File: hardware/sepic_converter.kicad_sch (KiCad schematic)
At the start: 8 parts, among them Q1 IRF640N, U1 TC4422

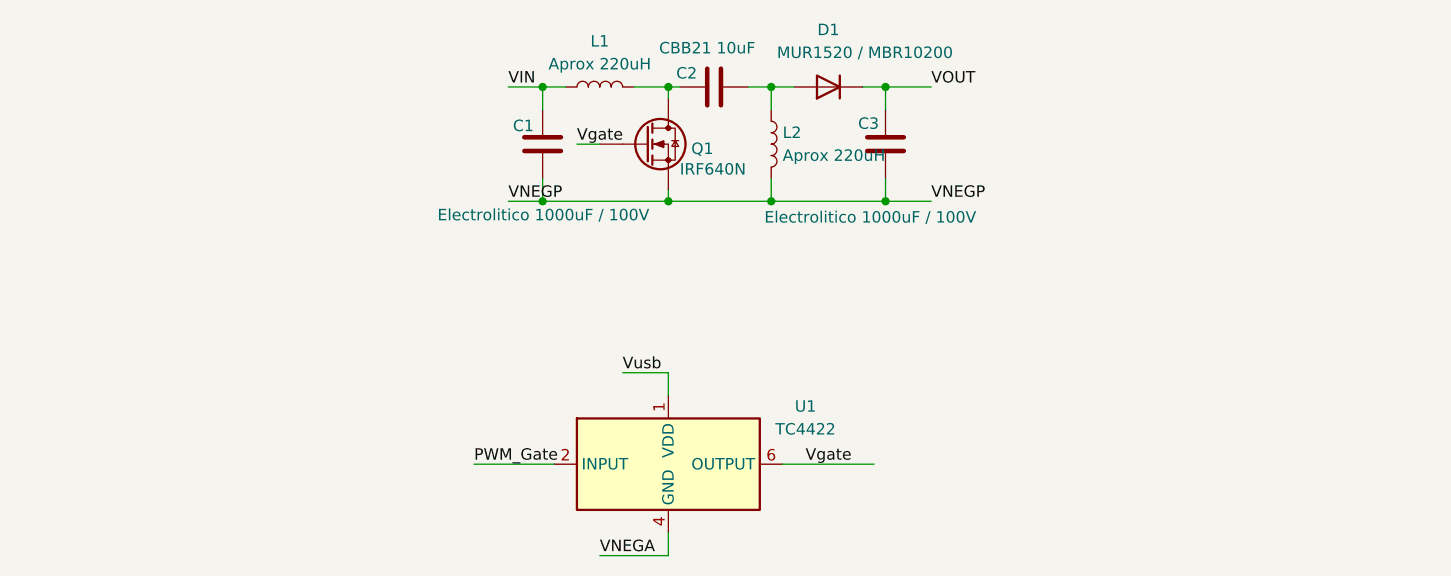
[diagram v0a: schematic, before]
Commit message: HW: Footprints, Descriptions and LCSC part number added to sch
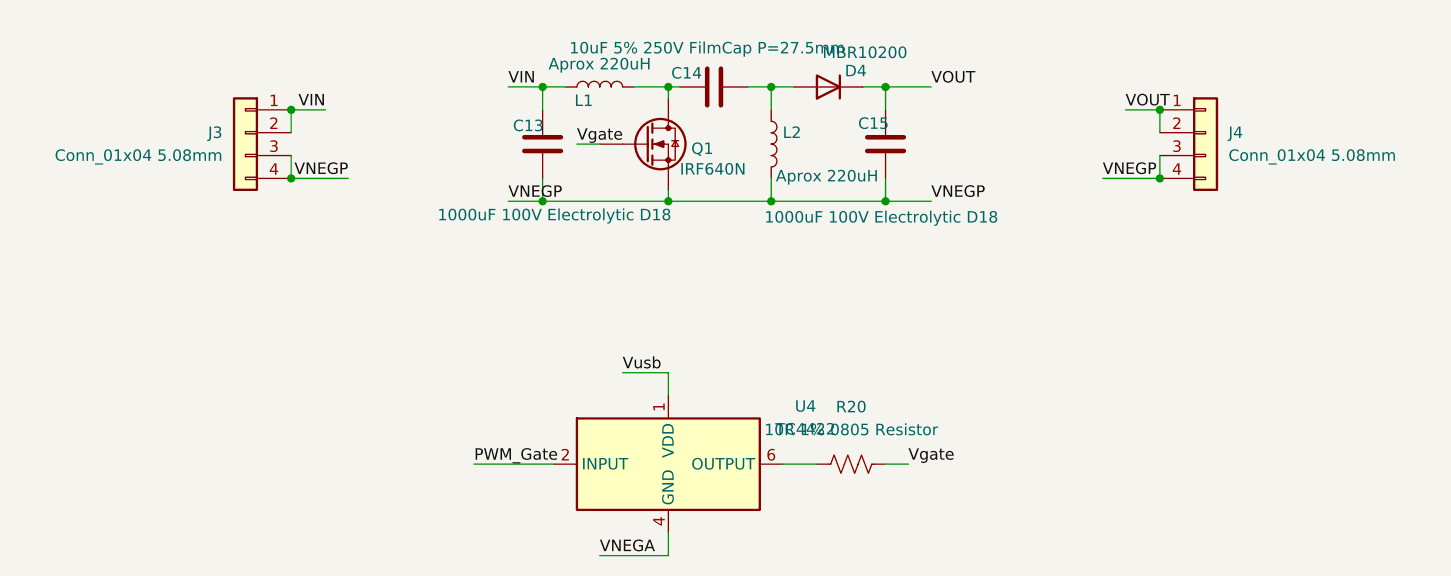
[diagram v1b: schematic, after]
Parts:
- added J3, J4: Conn_01x04 5.08mm, TerminalBlock_Phoenix:TerminalBlock_Phoenix_MKDS-1,5-4-5.08_1x04_P5.08mm_Horizontal, symbol Connector_Generic:Conn_01x04
- added R20: 10R 1% 0805 Resistor, Resistor_SMD:R_0805_2012Metric_Pad1.20x1.40mm_HandSolder, symbol Device:R_US
- C13: renamed from C1; value Electrolitico 1000uF / 100V -> 1000uF 100V Electrolytic D18; footprint (none) -> Capacitor_THT:CP_Radial_D18.0mm_P7.50mm; LCSC Part (none) -> C3445915; now left out of the parts list
- C14: renamed from C2; value CBB21 10uF -> 10uF 5% 250V FilmCap P=27.5mm; footprint (none) -> Capacitor_THT:C_Rect_L31.5mm_W17.0mm_P27.50mm_MKS4; LCSC Part (none) -> C5116053; now left out of the parts list
- C15: renamed from C3; value Electrolitico 1000uF / 100V -> 1000uF 100V Electrolytic D18; footprint (none) -> Capacitor_THT:CP_Radial_D18.0mm_P7.50mm; LCSC Part (none) -> C3445915; now left out of the parts list
- D4: renamed from D1; value MUR1520 / MBR10200 -> MBR10200; footprint (none) -> Package_TO_SOT_THT:TO-220F-3_Horizontal_TabDown; LCSC Part (none) -> C5795369; now left out of the parts list
- L1, L2: footprint (none) -> Inductor_THT:L_Toroid_Vertical_L25.4mm_W14.7mm_P12.20mm_Vishay_TJ5_BigPads; now left out of the parts list
- Q1: footprint (none) -> Package_TO_SOT_THT:TO-220-3_Horizontal_TabDown; LCSC Part (none) -> C2568; now left out of the parts list
- U4: renamed from U1; footprint Package_DIP:DIP-8_W7.62mm -> Package_SO:SOIC-8_5.3x5.3mm_P1.27mm; LCSC Part (none) -> C638566
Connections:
- net VIN: now also J3.1 (Pin_1), J3.2 (Pin_2)
- net VNEGP: now also J3.3 (Pin_3), J3.4 (Pin_4), J4.3 (Pin_3), J4.4 (Pin_4)
- net VOUT: now also J4.1 (Pin_1), J4.2 (Pin_2)
- net Vgate: now also R20.2; no longer U4.6 (OUTPUT), U4.7 (OUTPUT)
- new net: R20.1, U4.6 (OUTPUT), U4.7 (OUTPUT)
